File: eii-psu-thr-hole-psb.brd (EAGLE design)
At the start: 58 x 124 mm, 27 parts, among them IC2 7812DT

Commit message: Through hole version
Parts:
- added KK1, KK2, KK3: SK95V, joakim:SK95
- IC2: value 7812DT -> 7812TV; device linear:TO252 -> linear:TO220V
- U$1: value LD1085V -> LD1085V3; device joakim:TO263-3J -> joakim:TO220V-J
- U$2: value LM2991 -> LM2991V; device joakim:TO263-5J -> joakim:TO220-5V-J
- moved IC2 29.2 mm to (6.35, 17.1), turned to 90 degrees
- moved C2 22.2 mm to (31.1, 16.5), turned to 90 degrees
- moved R4 15.6 mm to (12.7, 52.1), turned to 0 degrees
- moved R1 14.7 mm to (19.7, 41.3), turned to 270 degrees
- moved C7 12.5 mm to (17.1, 45.7), turned to 0 degrees
- moved U$2 12.0 mm to (6.35, 59.7)
- moved C9 11.4 mm to (18.4, 59.7)
- moved C3 11.4 mm to (25.4, 59.7)
- moved U$1 10.6 mm to (6.35, 42.5)
- moved C6 10.3 mm to (23.5, 72.4)
- moved R2 10.3 mm to (14.6, 41.3), turned to 90 degrees
- moved C1 10.0 mm to (25.4, 42.5)
- moved R6 9.92 mm to (5.08, 71.1)
- moved R3 8.91 mm to (19.7, 52.1), turned to 180 degrees
- moved C5 8.03 mm to (23.5, 29.8), turned to 90 degrees
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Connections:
- net +12V: now also IC2.3; no longer IC2.2
- net +13.2V: no longer U$1.TAB
- net -14V: now also U$2.P$5; no longer U$2.5
- net -15V: now also U$2.P$3; no longer U$2.3, U$2.6
- net GND: now also IC2.2, U$2.P$2, U$2.P$4; no longer IC2.3, U$2.2, U$2.4
- net N$6: now also U$2.P$1; no longer U$2.1
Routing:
- net GND: track 295.3 -> 105.2 mm, vias 3 -> 0
- net +15V: track 122.9 -> 0.00 mm
- net -14V: track 117.2 -> 0.00 mm
- net +13.2V: track 77.0 -> 1.38 mm, vias 1 -> 0
- net -15V: track 40.1 -> 0.00 mm
- net N$6: track 33.4 -> 0.00 mm, vias 1 -> 0
- net N$2: track 22.5 -> 0.00 mm, vias 1 -> 0
- net +12V: track 16.3 -> 0.00 mm
- net N$5: track 8.81 -> 0.00 mm
- net N$1: track 5.56 -> 0.00 mm
- removed copper zone on layer 16, net GND
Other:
- board text added: "+5V"
- board text added: "+V2"
- board text added: "COM"
- board text added: "G"
- board text added: "L"
- board text added: "N"
- board text added: "V3"

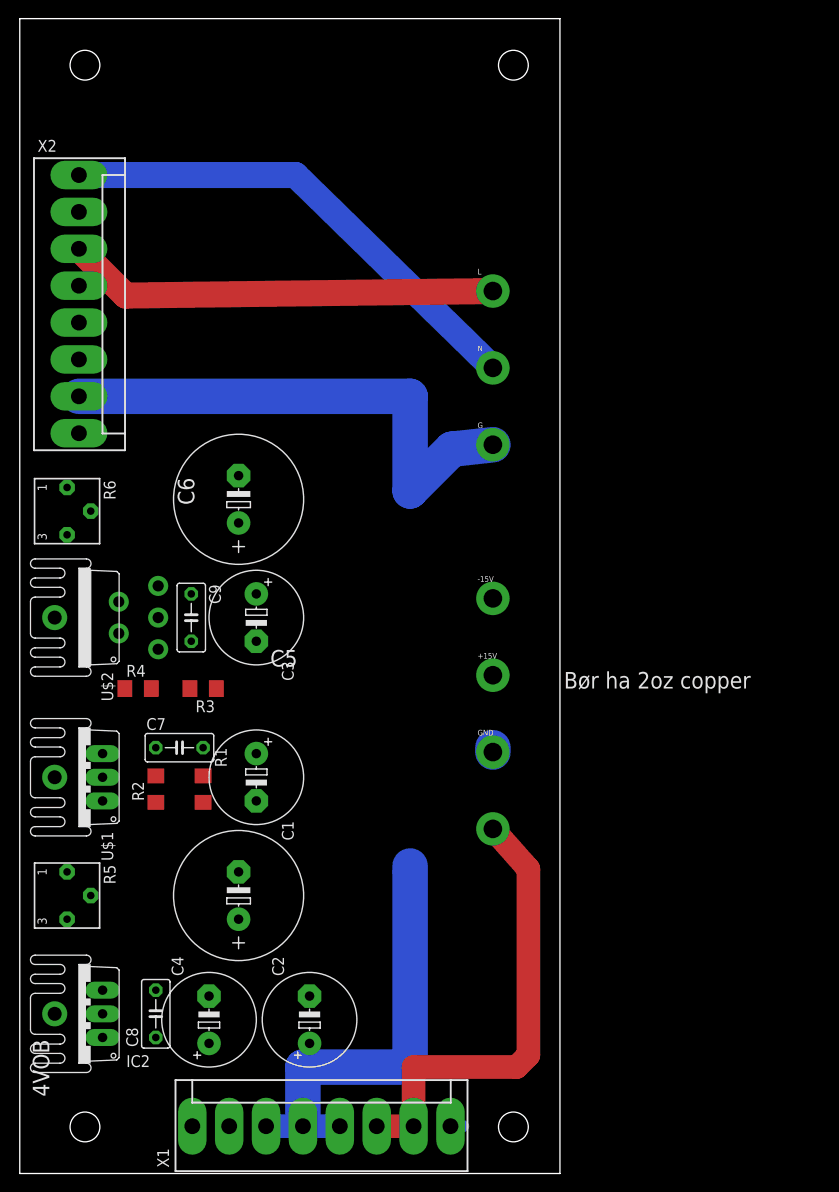
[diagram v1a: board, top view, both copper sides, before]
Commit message: Switched to through-hole resistors too
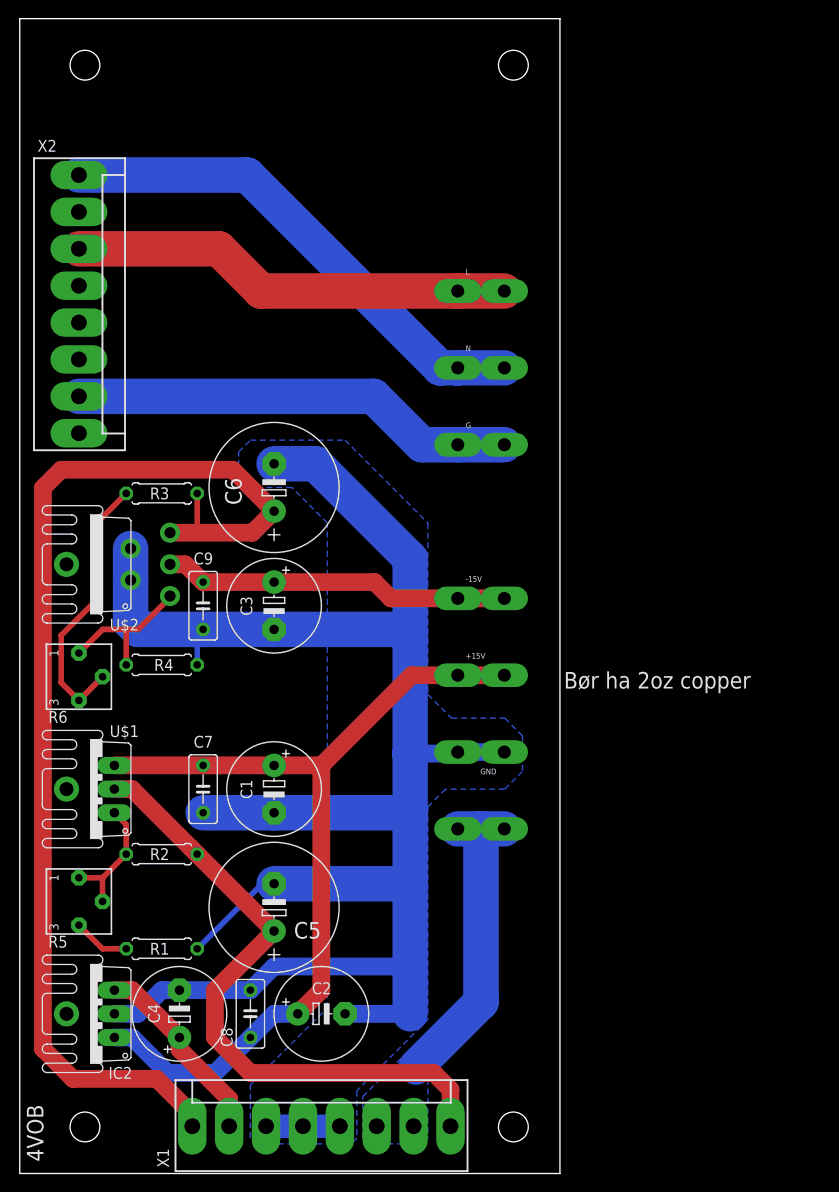
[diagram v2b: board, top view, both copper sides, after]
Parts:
- +15V, +5V, -15V, G, GND, L, N: value (none) -> PIN2F061.100; device SparkFun-Connectors:1X01_2MM -> con-faston:F061.100
- R1, R2, R3, R4: device rcl:R1206 -> rcl:0207/7
- moved R3 21.4 mm to (15.2, 73.0), turned to 0 degrees
- moved R6 17.8 mm to (6.35, 53.3)
- moved R1 17.7 mm to (15.2, 24.1), turned to 180 degrees
- moved C8 10.2 mm to (24.8, 17.1)
- moved R2 7.01 mm to (15.2, 34.3), turned to 0 degrees
- moved KK1 5.85 mm to (7.62, 65.4)
- moved U$2 5.85 mm to (7.62, 65.4)
- moved C7 5.12 mm to (19.7, 41.3), turned to 270 degrees
- moved C5 4.02 mm to (27.3, 28.6)
- moved C6 4.02 mm to (27.3, 73.7)
- moved R4 3.59 mm to (15.2, 54.6), turned to 180 degrees
- moved C4 3.24 mm to (17.1, 17.1)
- moved C1 2.29 mm to (27.3, 41.3)
- moved C3 2.29 mm to (27.3, 61.0)
- moved KK2 1.80 mm to (7.62, 41.3)
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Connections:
- new net G: G.A1, G.A2, X2.7
- net +15V: now also +15V.A1, +15V.A2; no longer +15V.1
- net +5V: now also +5V.A1, +5V.A2; no longer +5V.1
- net -15V: now also -15V.A1, -15V.A2; no longer -15V.1
- net GND: now also GND.A1, GND.A2; no longer G.1, GND.1, X2.7
- net LIVE: now also L.A1, L.A2; no longer L.1
- net NEUTRAL: now also N.A1, N.A2; no longer N.1
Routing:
- net -14V: track 0.00 -> 126.9 mm
- net GND: track 105.2 -> 217.5 mm
- net +15V: track 0.00 -> 97.5 mm
- net +13.2V: track 1.38 -> 69.0 mm
- net G: track 0.00 -> 47.8 mm
- net -15V: track 0.00 -> 37.4 mm
- net N$5: track 0.00 -> 29.5 mm
- net +12V: track 0.00 -> 20.8 mm
- net +5V: track 50.6 -> 33.5 mm
- net N$6: track 0.00 -> 16.2 mm
- net N$2: track 0.00 -> 13.6 mm
- net N$1: track 0.00 -> 6.13 mm
- net NEUTRAL: track 52.9 -> 54.3 mm
- net LIVE: track 46.5 -> 47.6 mm
- added copper zone on layer 16, net +5V
- added copper zone on layer 16, net GND

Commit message: Removed crossing neutral/live
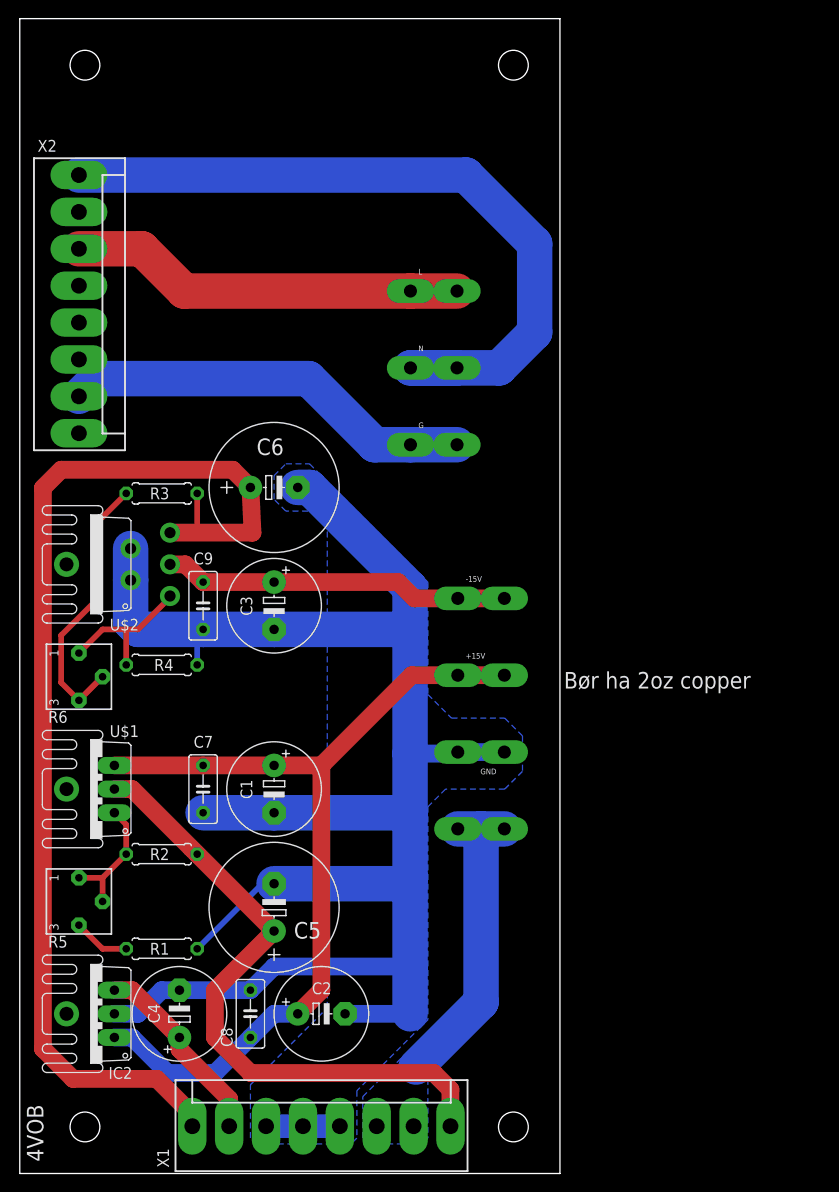
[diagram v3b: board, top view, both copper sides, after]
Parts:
- moved G 5.08 mm to (44.5, 78.2)
- moved L 5.08 mm to (44.5, 94.8)
- moved N 5.08 mm to (44.5, 86.5)
- turned C6 to 0 degrees
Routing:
- net NEUTRAL: track 54.3 -> 81.4 mm
- net GND: track 217.5 -> 212.0 mm
- net LIVE: track 47.6 -> 42.5 mm
- net G: track 47.8 -> 44.3 mm
- net -14V: track 126.9 -> 124.9 mm

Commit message: New heat sinks, better silk screen
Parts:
- added U$3: (no value), joakim:XONIK_LOGO_35
- KK1, KK2, KK3: value SK95V -> HEATSINKXSD; device joakim:SK95 -> joakim:XSD1226-005
- moved R3 21.6 mm to (15.2, 51.4)
- moved C4 4.49 mm to (20.3, 20.3)
- moved C5 4.45 mm to (27.3, 33.0)
- moved C1 4.45 mm to (27.3, 45.7)
- moved C7 4.45 mm to (19.7, 45.7)
- moved C8 4.07 mm to (27.3, 20.3)
- moved C2 3.70 mm to (34.3, 20.3)
- moved R1 3.18 mm to (15.2, 27.3)
- moved R2 3.18 mm to (15.2, 31.1)
- moved R4 0.63 mm to (15.2, 55.2)
- renumbered U$1 to IC1, U$2 to IC3
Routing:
- net N$5: track 29.5 -> 7.25 mm
- net -14V: track 124.9 -> 135.4 mm
- net GND: track 212.0 -> 221.3 mm
- net +5V: track 33.5 -> 40.6 mm
- net +12V: track 20.8 -> 24.5 mm
- net +15V: track 97.5 -> 100.9 mm
- net N$2: track 13.6 -> 16.1 mm
- net N$6: track 16.2 -> 13.8 mm
- net +13.2V: track 69.0 -> 71.3 mm
- net N$1: track 6.13 -> 5.34 mm
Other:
- board text added: "+12"
- board text added: "+13.2"
- board text added: "-14"
- board text added: "Emulator II Voltage regulators v1.0"
- board text added: "GND"
- board text added: "Trim -14V"
- board text added: "Trim 13.2V"

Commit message: Tweaks after uploading to JLCPCB
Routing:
- net GND: track 221.3 -> 219.2 mm
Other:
- board text added: "+15V"
- board text added: "-15V"
- board text added: "MEAN WELL RT-85C"

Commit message: Added all parts except regulators
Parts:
- +15V, +5V, -15V, G, GND, L, N: value PIN2F061.100 -> FLATSTIFT; device con-faston:F061.100 -> joakim:FLATSTIFT
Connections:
- net +15V: now also +15V.F, +15V.F2; no longer +15V.A1, +15V.A2
- net +5V: now also +5V.F, +5V.F2; no longer +5V.A1, +5V.A2
- net -15V: now also -15V.F, -15V.F2; no longer -15V.A1, -15V.A2
- net G: now also G.F, G.F2; no longer G.A1, G.A2
- net GND: now also GND.F, GND.F2; no longer GND.A1, GND.A2
- net LIVE: now also L.F, L.F2; no longer L.A1, L.A2
- net NEUTRAL: now also N.F, N.F2; no longer N.A1, N.A2
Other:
- board text removed: "Bør ha 2oz copper"
